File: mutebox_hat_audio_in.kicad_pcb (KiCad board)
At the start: 2 copper layers, 65 x 56 mm, 32 parts, among them IC1 WM8804GEDS_V, J1 GPIO, J2 AFBR-2624Z, U1 CAT24C256, U2 74LVC157, U3 PCM1862DBT, Y1 12.288 MHz

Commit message: Started on PCB
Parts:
- moved R10 38.8 mm to (110.5, 54.5)
- moved R6 24.1 mm to (162.5, 70.0)
- moved R4 23.6 mm to (162.5, 65.5)
- moved R5 21.5 mm to (162.0, 74.5)
- moved C8 20.3 mm to (148.5, 55.5)
- moved C9 15.6 mm to (147.0, 63.5)
- moved U1 12.2 mm to (141.5, 73.9)
- moved R1 11.1 mm to (139.5, 54.5)
- moved R8 9.93 mm to (135.5, 66.0)
- moved R9 9.65 mm to (142.0, 59.5)
- moved C4 9.07 mm to (129.2, 56.5)
- moved C7 8.42 mm to (129.2, 66.0)
- moved R2 8.32 mm to (147.5, 73.3), turned to -90 degrees
- moved C1 8.22 mm to (129.0, 70.0)
- moved C6 7.53 mm to (129.0, 79.0)
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
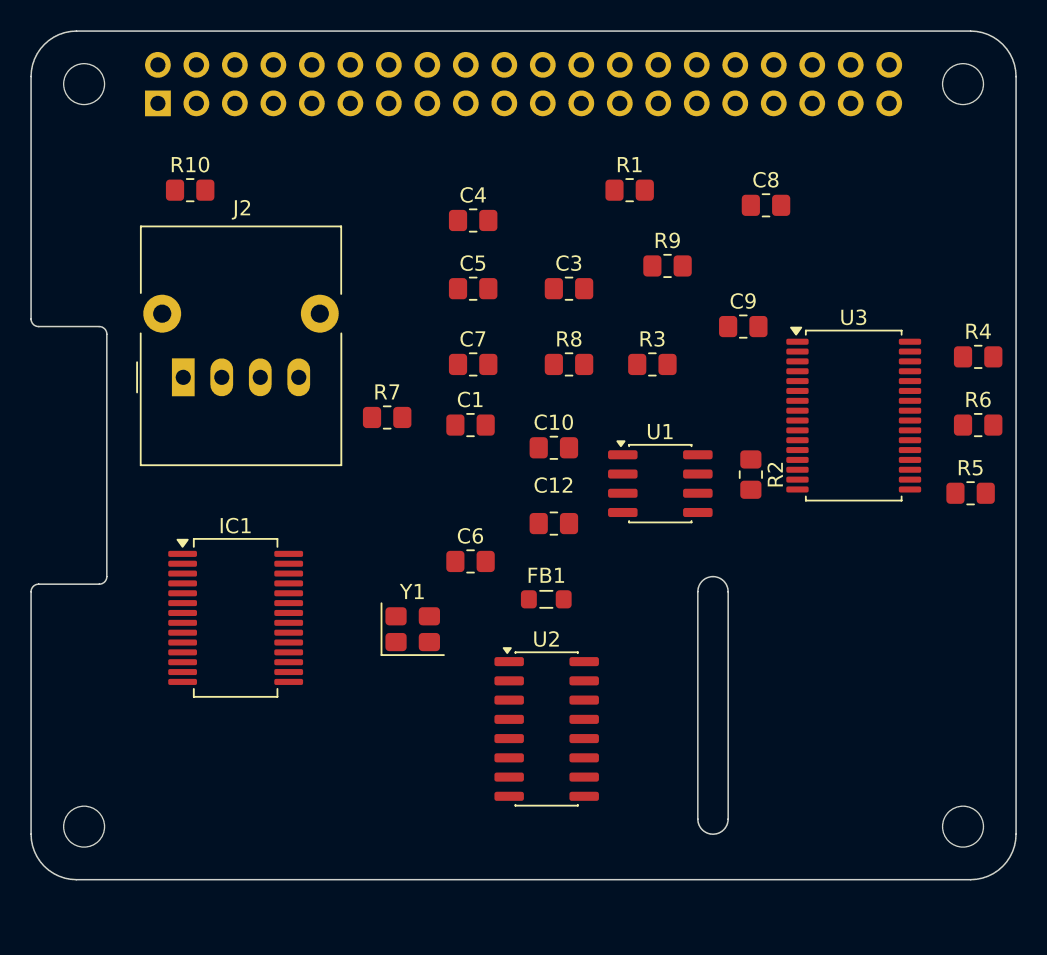
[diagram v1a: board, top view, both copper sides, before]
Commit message: Started positioning of components
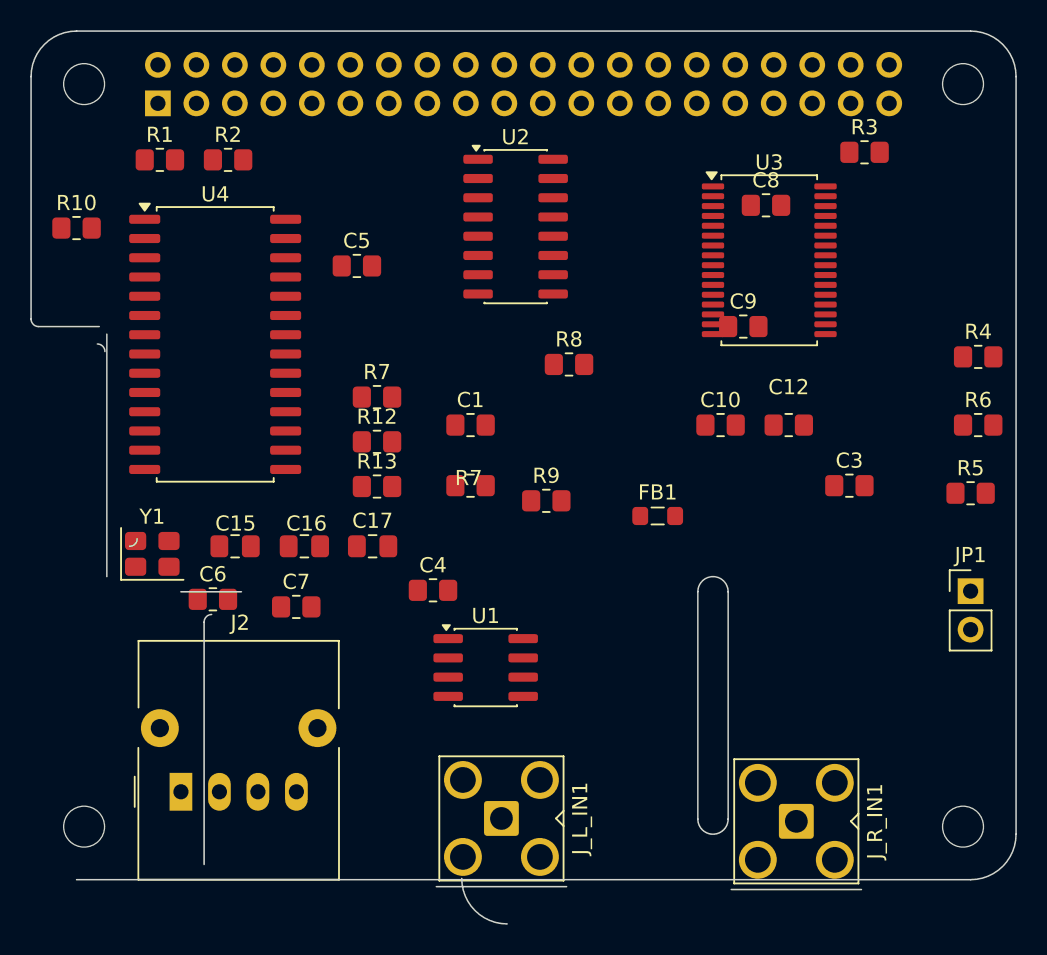
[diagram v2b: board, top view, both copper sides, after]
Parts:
- removed IC1: WM8804GEDS_V, Package_SO:SSOP-28_5.3x10.2mm_P0.65mm
- added C15: 100nF, Capacitor_SMD:C_0805_2012Metric_Pad1.18x1.45mm_HandSolder, F.Cu at (113.5, 78.0)
- added C16: 100nF, Capacitor_SMD:C_0805_2012Metric_Pad1.18x1.45mm_HandSolder, F.Cu at (118.0, 78.0)
- added C17: 100nF, Capacitor_SMD:C_0805_2012Metric_Pad1.18x1.45mm_HandSolder, F.Cu at (122.5, 78.0)
- added JP1: ID_WP, Connector_PinHeader_2.54mm:PinHeader_1x02_P2.54mm_Vertical, F.Cu at (162.0, 81.0)
- added J_L_IN1: Conn_Coaxial, Connector_Coaxial:SMA_Amphenol_901-143_Horizontal, F.Cu at (131.0, 96.0)
- added J_R_IN1: Conn_Coaxial, Connector_Coaxial:SMA_Amphenol_901-143_Horizontal, F.Cu at (150.5, 96.2)
- added R12: 4.7k, Resistor_SMD:R_0805_2012Metric_Pad1.20x1.40mm_HandSolder, F.Cu at (122.8, 71.1)
- added R13: 4.7k, Resistor_SMD:R_0805_2012Metric_Pad1.20x1.40mm_HandSolder, F.Cu at (122.8, 74.1)
- added R7: 10k, Resistor_SMD:R_0805_2012Metric_Pad1.20x1.40mm_HandSolder, F.Cu at (122.8, 68.2)
- added U4: DIR9001PW, Package_SO:SOIC-28W_7.5x17.9mm_P1.27mm, F.Cu at (112.2, 64.7)
- C4: value C -> 10uF
- moved R2 40.3 mm to (113.0, 52.5), turned to 0 degrees
- moved U2 33.2 mm to (132.0, 56.9)
- moved R1 31.1 mm to (108.5, 52.5)
- moved J2 27.4 mm to (109.9, 94.2)
- moved C4 24.5 mm to (126.5, 80.9)
- moved C3 22.6 mm to (154.0, 74.0)
- moved C7 19.8 mm to (117.5, 82.0)
- moved R3 19.8 mm to (155.0, 52.0)
- moved Y1 17.9 mm to (108.0, 78.5)
- moved R9 17.4 mm to (134.0, 75.0)
- moved C6 17.2 mm to (112.0, 81.5)
- moved C12 16.8 mm to (150.0, 70.0)
- moved U1 16.7 mm to (130.0, 86.0)
- moved U3 11.7 mm to (148.7, 59.1)
- moved C10 11.1 mm to (145.5, 70.0)
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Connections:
- net ID_SC renamed ID_SCL
- J1 pad 38: /GPIO20/PCM.DIN -> I2S_DOUT
- U2 pad 10: GND -> ADC_SDOUT
- U2 pad 11: GND -> TOSLINK_DOUT
- U2 pad 2: ADC_SDOUT -> TOSLINK_BCLK
- U2 pad 3: SPDIF_SDOUT -> ADC_BCLK
- U2 pad 4: I2S_SDIN -> I2S_BCLK
- U2 pad 5: GND -> TOSLINK_LRCLK
- U2 pad 6: GND -> ADC_LRCLK
- U2 pad 7: unconnected-(U2-Zb-Pad7) -> I2S_LRCLK
- U2 pad 9: unconnected-(U2-Zc-Pad9) -> I2S_DOUT
- U3 pad 16: I2S_LRCLK -> ADC_LRCLK
- U3 pad 17: I2S_BCLK -> ADC_BCLK
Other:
- board size 65 x 56 mm -> 65 x 58.9 mm

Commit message: Laid out most components
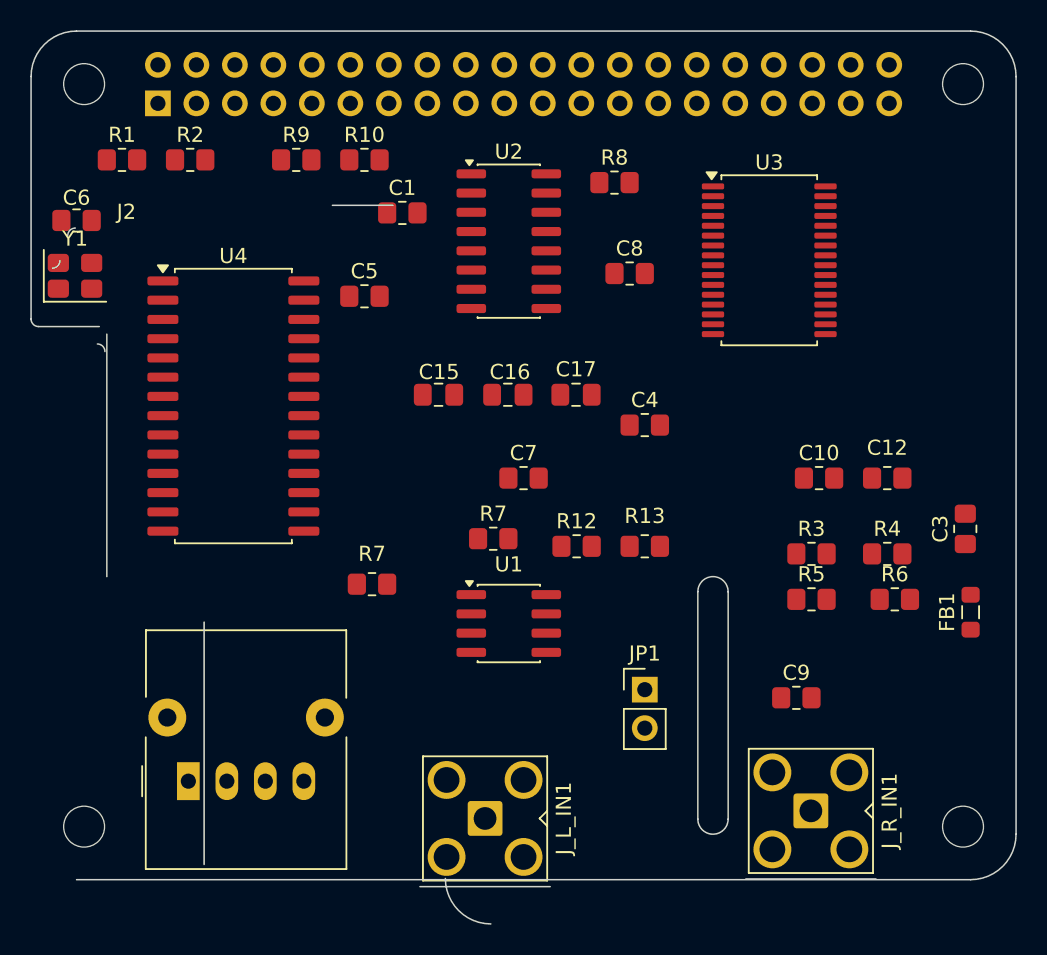
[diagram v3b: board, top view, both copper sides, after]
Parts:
- moved R9 27.9 mm to (117.5, 52.5)
- moved R3 26.7 mm to (151.5, 78.5)
- moved C6 26.6 mm to (103.0, 56.5)
- moved C9 24.7 mm to (150.5, 88.0)
- moved JP1 22.5 mm to (140.5, 87.5)
- moved FB1 21.6 mm to (162.0, 82.3), turned to 90 degrees
- moved R10 19.5 mm to (122.0, 52.5)
- moved Y1 19.0 mm to (102.9, 60.1)
- moved R13 18.1 mm to (140.5, 78.0)
- moved C4 17.7 mm to (140.5, 70.0)
- moved C7 17.2 mm to (132.5, 73.5)
- moved C16 16.7 mm to (131.5, 68.0)
- moved C17 16.7 mm to (136.0, 68.0)
- moved C15 16.7 mm to (126.9, 68.0)
- moved R12 14.9 mm to (136.0, 78.0)
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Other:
- outline, holes or cut-outs redrawn

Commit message: Added SPDIF/TOSLINK footprint
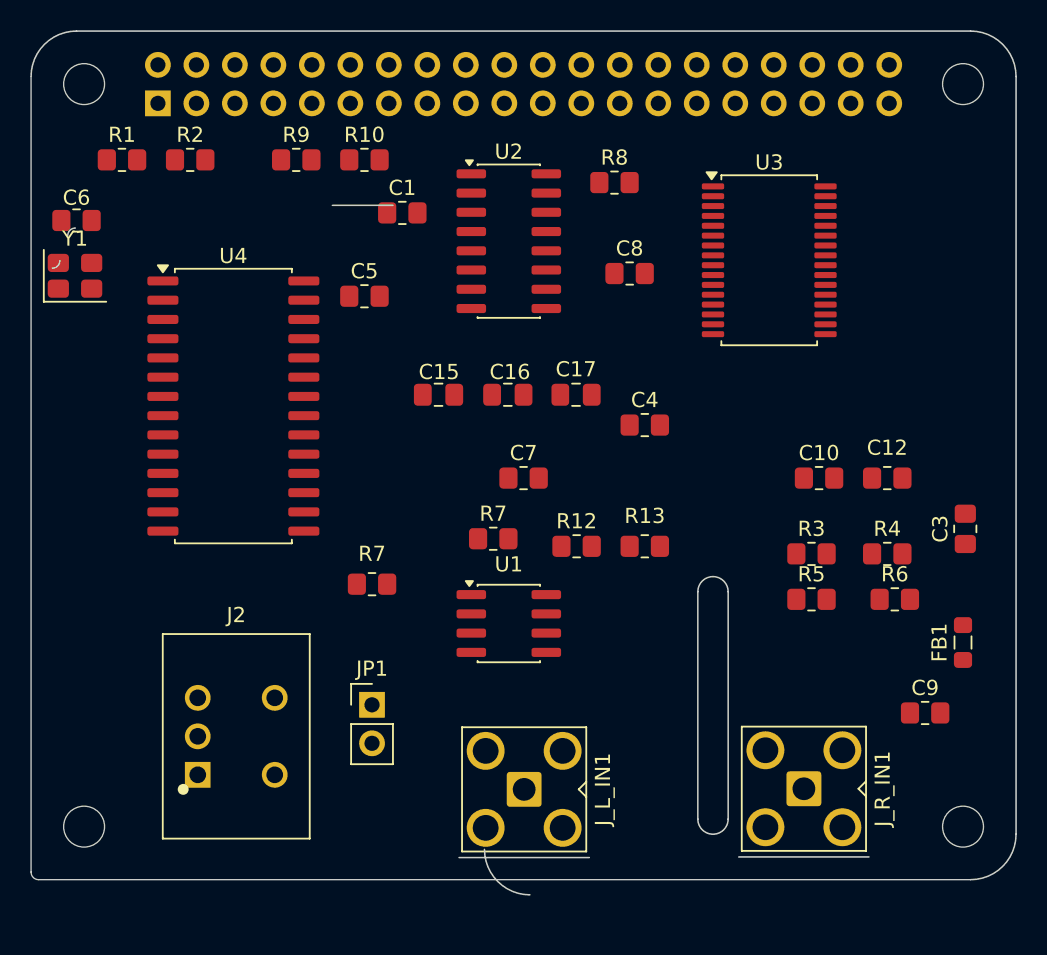
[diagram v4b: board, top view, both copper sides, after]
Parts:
- J2: footprint OptoDevice:Toshiba_TORX170_TORX173_TORX193_TORX194 -> Connector_Audio:PLR237-T10BK
- moved JP1 18.0 mm to (122.5, 88.5)
- moved C9 8.56 mm to (159.0, 89.0)
- moved J2 4.33 mm to (113.5, 90.5)
- moved J_L_IN1 3.22 mm to (132.5, 94.0)
- moved FB1 2.06 mm to (161.5, 84.3)
- moved J_R_IN1 1.53 mm to (151.0, 94.0)
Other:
- board size 65 x 58.9 mm -> 65 x 57 mm

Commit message: Added new footprints for TOSLINK and RCA.  Fixed outer edge. PCB ready to add routes.
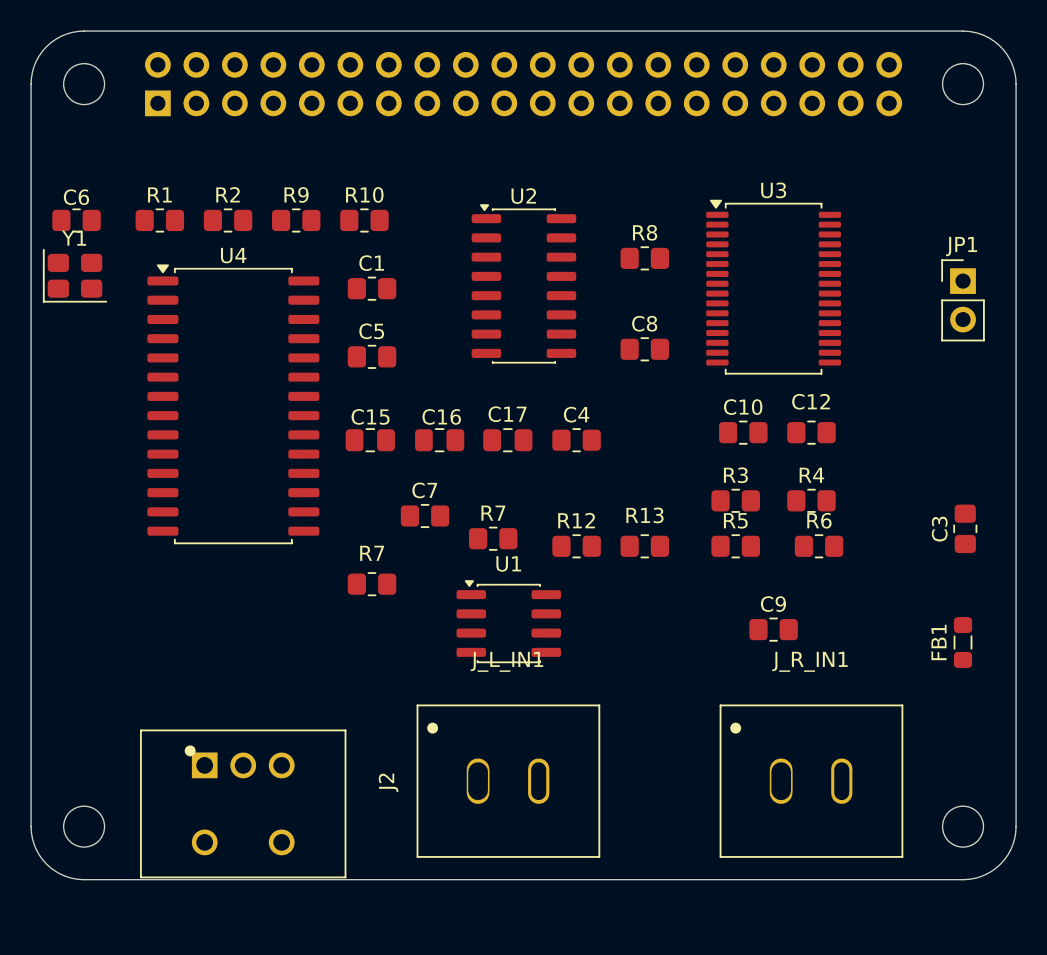
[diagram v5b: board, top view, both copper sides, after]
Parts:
- J2: value AFBR-2624Z -> PLR237/T10BK
- J_L_IN1, J_R_IN1: footprint Connector_Coaxial:SMA_Amphenol_901-143_Horizontal -> Connector_Audio:RCJ-043
- moved JP1 48.0 mm to (161.5, 60.5)
- moved C9 11.4 mm to (149.0, 83.5)
- moved C7 6.96 mm to (126.0, 76.0)
- moved R3 6.10 mm to (146.5, 75.0)
- moved R4 6.10 mm to (151.5, 75.0)
- moved R5 6.10 mm to (146.5, 78.0)
- moved R6 6.10 mm to (152.0, 78.0)
- moved C10 5.83 mm to (147.0, 70.5)
- moved C12 5.83 mm to (151.5, 70.5)
- moved C15 5.41 mm to (122.4, 71.0)
- moved C16 5.41 mm to (127.0, 71.0)
- moved C17 5.41 mm to (131.5, 71.0)
- moved C1 5.39 mm to (122.5, 61.0)
- moved R8 5.39 mm to (140.5, 59.0)
- moved C8 5.10 mm to (140.5, 65.0)
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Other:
- board size 65 x 57 mm -> 65 x 56 mm
- board text removed: "CAMERA (OPTIONAL)"
- board text removed: "Extend PCB edge 0.5mm if using SMT header"

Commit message: Added routes for crystal and part of toslink
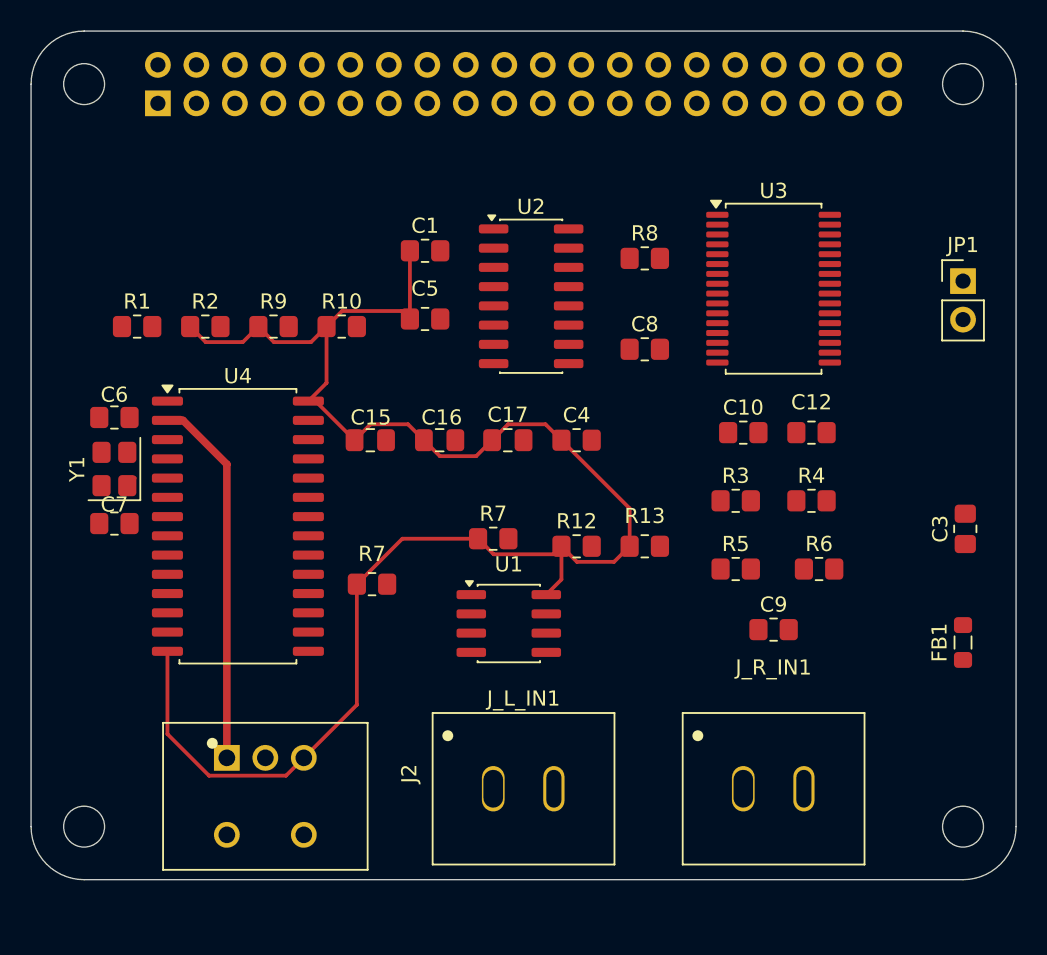
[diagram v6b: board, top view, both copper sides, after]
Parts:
- moved C7 20.5 mm to (105.5, 76.5)
- moved C6 13.2 mm to (105.5, 69.5)
- moved Y1 13.0 mm to (105.5, 72.9), turned to 90 degrees
- moved U4 7.94 mm to (113.7, 76.7)
- moved R1 7.16 mm to (107.0, 63.5)
- moved R10 7.16 mm to (120.5, 63.5)
- moved R2 7.16 mm to (111.5, 63.5)
- moved R9 7.16 mm to (116.0, 63.5)
- moved C1 4.30 mm to (126.0, 58.5)
- moved C5 4.30 mm to (126.0, 63.0)
- moved J_R_IN1 2.55 mm to (149.0, 94.0)
- moved J2 1.54 mm to (115.5, 94.5)
- moved R5 1.50 mm to (146.5, 79.5)
- moved R6 1.50 mm to (152.0, 79.5)
- moved J_L_IN1 1.12 mm to (132.5, 94.0)
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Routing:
- net +3V3: track 0.00 -> 109.3 mm
- net /Audio Inputs/SPDIF_IN: track 0.00 -> 24.5 mm
- net Net-(U4-XO): track 0.00 -> 0.71 mm
- net Net-(U4-XI): track 0.00 -> 0.61 mm
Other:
- board text removed: "DISPLAY (OPTIONAL)"

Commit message: Got ground layers/fill zones done
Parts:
- moved R1 33.5 mm to (140.5, 62.0), turned to -90 degrees
- moved C15 26.2 mm to (148.5, 69.5), turned to -90 degrees
- moved C8 21.0 mm to (140.5, 86.0)
- moved U1 20.7 mm to (132.5, 62.4)
- moved U2 18.3 mm to (133.0, 79.8)
- moved R8 18.1 mm to (138.5, 77.0), turned to -90 degrees
- moved U3 18.0 mm to (148.5, 79.0)
- moved C5 12.5 mm to (137.0, 57.0)
- moved R13 11.7 mm to (132.5, 69.5), turned to -90 degrees
- moved R3 10.8 mm to (155.5, 81.0), turned to 180 degrees
- moved C12 9.55 mm to (142.0, 69.5), turned to -90 degrees
- moved C9 9.55 mm to (142.0, 77.0), turned to -90 degrees
- moved R12 9.55 mm to (126.5, 79.0), turned to 90 degrees
- moved R5 9.12 mm to (155.5, 78.0), turned to 180 degrees
- moved C17 8.11 mm to (123.5, 69.5), turned to -90 degrees
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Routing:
- net +3V3: track 109.3 -> 62.3 mm
- net GND: vias 0 -> 9
- added copper zone on B.Cu, net GND
- added copper zone on F.Cu, net GND
